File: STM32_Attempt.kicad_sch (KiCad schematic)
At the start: 29 parts, among them J1 Conn_01x04_Male, J2 Conn_01x04_Male, J3 Conn_01x04_Male, J4 Conn_01x04_Male, J5 USB_B_Micro, SW1 SW_SPDT, U1 AMS1117-3.3, U2 STM32F103C8T6, Y1 16Mhz

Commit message: added some leds
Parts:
- added D? (x4): WS2812B, LED_SMD:LED_WS2812B_PLCC4_5.0x5.0mm_P3.2mm, symbol LED:WS2812B
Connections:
- new net: D?.2 (DOUT), D?.4 (DIN) (x3)
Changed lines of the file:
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@@
+    (stroke (width 0) (type default) (color 0 0 0 0))
+  )
+  (wire (pts (xy 38.1 144.78) (xy 40.64 144.78))
     (stroke (width 0) (type default) (color 0 0 0 0))
   )
@@
     (stroke (width 0) (type default) (color 0 0 0 0))
   )
+  (wire (pts (xy 20.32 144.78) (xy 22.86 144.78))
+    (stroke (width 0) (type default) (color 0 0 0 0))
+  )
   (wire (pts (xy 111.76 69.85) (xy 123.19 69.85))
     (stroke (width 0) (type default) (color 0 0 0 0))
@@
   )
   (polyline (pts (xy 20.32 78.74) (xy 69.85 78.74))
+    (stroke (width 0) (type default) (color 0 0 0 0))
+  )
+  (wire (pts (xy 55.88 144.78) (xy 58.42 144.78))
     (stroke (width 0) (type default) (color 0 0 0 0))
   )
@@
     )
     (pin "1")
+  )
+  (symbol (lib_id "LED:WS2812B") (at 66.04 144.78 0) (unit 1)
+    (in_bom yes) (on_board yes) (fields_autoplaced)
+    (property "Reference" "D?" (id 0) (at 77.47 140.4493 0))
+    (property "Value" "WS2812B" (id 1) (at 77.47 142.9893 0))
+    (property "Footprint" "LED_SMD:LED_WS2812B_PLCC4_5.0x5.0mm_P3.2mm" (id 2) (at 67.31 152.4 0)
+      (effects (font (size 1.27 1.27)) (justify left top) hide)
+    )
+    (property "Datasheet" "https://cdn-shop.adafruit.com/datasheets/WS2812B.pdf" (id 3) (at 68.58 154.305 0)
+      (effects (font (size 1.27 1.27)) (justify left top) hide)
+    )
+    (pin "1")
+    (pin "2")
+    (pin "3")
+    (pin "4")
   )
   (symbol (lib_id "power:+3.3V") (at 116.84 139.7 0) (unit 1)
@@
     (pin "1")
   )
+  (symbol (lib_id "LED:WS2812B") (at 30.48 144.78 0) (unit 1)
+    (in_bom yes) (on_board yes) (fields_autoplaced)
+    (property "Reference" "D?" (id 0) (at 41.91 140.4493 0))
+    (property "Value" "WS2812B" (id 1) (at 41.91 142.9893 0))
+    (property "Footprint" "LED_SMD:LED_WS2812B_PLCC4_5.0x5.0mm_P3.2mm" (id 2) (at 31.75 152.4 0)
+      (effects (font (size 1.27 1.27)) (justify left top) hide)
+    )
+    (property "Datasheet" "https://cdn-shop.adafruit.com/datasheets/WS2812B.pdf" (id 3) (at 33.02 154.305 0)
+      (effects (font (size 1.27 1.27)) (justify left top) hide)
+    )
+    (pin "1")
+    (pin "2")
+    (pin "3")
+    (pin "4")
+  )
   (symbol (lib_id "Connector:Conn_01x04_Male") (at 109.22 123.19 0) (unit 1)
     (in_bom yes) (on_board yes)
@@
     (property "Datasheet" "~" (id 3) (at 109.22 123.19 0)
       (effects (font (size 1.27 1.27)) hide)
+    )
+    (pin "1")
+    (pin "2")
+    (pin "3")
+    (pin "4")
+  )
+  (symbol (lib_id "LED:WS2812B") (at 12.7 144.78 0) (unit 1)
+    (in_bom yes) (on_board yes) (fields_autoplaced)
+    (property "Reference" "D?" (id 0) (at 24.13 140.4493 0))
+    (property "Value" "WS2812B" (id 1) (at 24.13 142.9893 0))
+    (property "Footprint" "LED_SMD:LED_WS2812B_PLCC4_5.0x5.0mm_P3.2mm" (id 2) (at 13.97 152.4 0)
+      (effects (font (size 1.27 1.27)) (justify left top) hide)
+    )
+    (property "Datasheet" "https://cdn-shop.adafruit.com/datasheets/WS2812B.pdf" (id 3) (at 15.24 154.305 0)
+      (effects (font (size 1.27 1.27)) (justify left top) hide)
     )
     (pin "1")
@@
     (pin "2")
   )
+  (symbol (lib_id "LED:WS2812B") (at 48.26 144.78 0) (unit 1)
+    (in_bom yes) (on_board yes) (fields_autoplaced)
+    (property "Reference" "D?" (id 0) (at 59.69 140.4493 0))
+    (property "Value" "WS2812B" (id 1) (at 59.69 142.9893 0))
+    (property "Footprint" "LED_SMD:LED_WS2812B_PLCC4_5.0x5.0mm_P3.2mm" (id 2) (at 49.53 152.4 0)
+      (effects (font (size 1.27 1.27)) (justify left top) hide)
+    )
+    (property "Datasheet" "https://cdn-shop.adafruit.com/datasheets/WS2812B.pdf" (id 3) (at 50.8 154.305 0)
+      (effects (font (size 1.27 1.27)) (justify left top) hide)
+    )
+    (pin "1")
+    (pin "2")
+    (pin "3")
+    (pin "4")
+  )
   (symbol (lib_id "Device:Crystal_GND24") (at 127 87.63 0) (unit 1)
     (in_bom yes) (on_board yes)
@@
       (reference "D1") (unit 1) (value "RED") (footprint "LED_SMD:LED_0603_1608Metric")
     )
+    (path "/4eff6cc9-a752-4648-bcf8-9735cd35d6cf"
+      (reference "D?") (unit 1) (value "WS2812B") (footprint "LED_SMD:LED_WS2812B_PLCC4_5.0x5.0mm_P3.2mm")
+    )
+    (path "/b643fd5e-31e0-4018-ad35-66a9d8220cd2"
+      (reference "D?") (unit 1) (value "WS2812B") (footprint "LED_SMD:LED_WS2812B_PLCC4_5.0x5.0mm_P3.2mm")
+    )
+    (path "/b718910d-5e7e-4b6b-8296-0ffdf283276d"
+      (reference "D?") (unit 1) (value "WS2812B") (footprint "LED_SMD:LED_WS2812B_PLCC4_5.0x5.0mm_P3.2mm")
+    )
+    (path "/f18ae84f-67e5-42ce-a84a-119c99da9cea"
+      (reference "D?") (unit 1) (value "WS2812B") (footprint "LED_SMD:LED_WS2812B_PLCC4_5.0x5.0mm_P3.2mm")
+    )
     (path "/747181f7-c7c1-464c-a385-7c72b8faff1e"

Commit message: LED Matrix before markings
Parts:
- removed D? (x3): WS2812B, LED_SMD:LED_WS2812B_PLCC4_5.0x5.0mm_P3.2mm, symbol LED:WS2812B
- added D10, D11, D12, D13, D14, D15, D16, D17, D18, D19, D20, D21, D22, D23, D24, D25, D26, D27, D28, D29, D3, D30, D31, D32, D33, D34, D35, D36, D37, D38, D39, D4, D40, D41, D42, D43, D44, D45, D46, D47, D48, D49, D5, D50, D51, D52, D53, D54, D55, D56, D57, D58, D59, D6, D60, D61, D62, D63, D64, D65, D7, D8, D9: WS2812B, LED_SMD:LED_WS2812B_PLCC4_5.0x5.0mm_P3.2mm, symbol LED:WS2812B
- added J6: Conn_01x02, symbol Connector_Generic:Conn_01x02
- gave numbers to parts that had none: 1
- renumbered C7 to C10, C8 to C3, C3 to C4, C9 to C5, C4 to C6, C5 to C7, C10 to C8, C6 to C9, J3 to J2, J2 to J3
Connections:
- net GND: now also D2.3 (VSS), D10.3 (VSS), D11.3 (VSS), D12.3 (VSS), D13.3 (VSS), D14.3 (VSS), D15.3 (VSS), D16.3 (VSS), D17.3 (VSS), D18.3 (VSS), D19.3 (VSS), D20.3 (VSS), D21.3 (VSS), D22.3 (VSS), D23.3 (VSS), D24.3 (VSS), D25.3 (VSS), D26.3 (VSS), D27.3 (VSS), D28.3 (VSS), D29.3 (VSS), D3.3 (VSS), D30.3 (VSS), D31.3 (VSS), D32.3 (VSS), D33.3 (VSS), D34.3 (VSS), D35.3 (VSS), D36.3 (VSS), D37.3 (VSS), D38.3 (VSS), D39.3 (VSS), D4.3 (VSS), D40.3 (VSS), D41.3 (VSS), D42.3 (VSS), D43.3 (VSS), D44.3 (VSS), D45.3 (VSS), D46.3 (VSS), D47.3 (VSS), D48.3 (VSS), D49.3 (VSS), D5.3 (VSS), D50.3 (VSS), D51.3 (VSS), D52.3 (VSS), D53.3 (VSS), D54.3 (VSS), D55.3 (VSS), D56.3 (VSS), D57.3 (VSS), D58.3 (VSS), D59.3 (VSS), D6.3 (VSS), D60.3 (VSS), D61.3 (VSS), D62.3 (VSS), D63.3 (VSS), D64.3 (VSS), D65.3 (VSS), D7.3 (VSS), D8.3 (VSS), D9.3 (VSS), J6.2 (Pin_2)
- net at D2.2 (DOUT): now also D10.4 (DIN)
- net 5V: now reaches D2.1 (VDD)
- net 5V: now also D10.1 (VDD), D11.1 (VDD), D12.1 (VDD), D13.1 (VDD), D14.1 (VDD), D15.1 (VDD), D16.1 (VDD), D17.1 (VDD), D18.1 (VDD), D19.1 (VDD), D20.1 (VDD), D21.1 (VDD), D22.1 (VDD), D23.1 (VDD), D24.1 (VDD), D25.1 (VDD), D26.1 (VDD), D27.1 (VDD), D28.1 (VDD), D29.1 (VDD), D3.1 (VDD), D30.1 (VDD), D31.1 (VDD), D32.1 (VDD), D33.1 (VDD), D34.1 (VDD), D35.1 (VDD), D36.1 (VDD), D37.1 (VDD), D38.1 (VDD), D39.1 (VDD), D4.1 (VDD), D40.1 (VDD), D41.1 (VDD), D42.1 (VDD), D43.1 (VDD), D44.1 (VDD), D45.1 (VDD), D46.1 (VDD), D47.1 (VDD), D48.1 (VDD), D49.1 (VDD), D5.1 (VDD), D50.1 (VDD), D51.1 (VDD), D52.1 (VDD), D53.1 (VDD), D54.1 (VDD), D55.1 (VDD), D56.1 (VDD), D57.1 (VDD), D58.1 (VDD), D59.1 (VDD), D6.1 (VDD), D60.1 (VDD), D61.1 (VDD), D62.1 (VDD), D63.1 (VDD), D64.1 (VDD), D65.1 (VDD), D7.1 (VDD), D8.1 (VDD), D9.1 (VDD)
- net at D2.4 (DIN): now also U2.29 (PA8)
- new net: D16.2 (DOUT), D24.4 (DIN)
- new net: D16.4 (DIN), D8.2 (DOUT)
- new net: D7.2 (DOUT), D8.4 (DIN)
- new net: D15.2 (DOUT), D7.4 (DIN)
- new net: D33.4 (DIN), D41.2 (DOUT)
- new net: D41.4 (DIN), D49.2 (DOUT)
- new net: D47.4 (DIN), D55.2 (DOUT)
- new net: D55.4 (DIN), D63.2 (DOUT)
- new net: D24.2 (DOUT), D32.4 (DIN)
- new net: D37.4 (DIN), D45.2 (DOUT)
- new net: D45.4 (DIN), D53.2 (DOUT)
- new net: D49.4 (DIN), D57.2 (DOUT)
- new net: D11.4 (DIN), D19.2 (DOUT)
- new net: D19.4 (DIN), D27.2 (DOUT)
- new net: D29.4 (DIN), D37.2 (DOUT)
- new net: D42.2 (DOUT), D50.4 (DIN)
- new net: D34.2 (DOUT), D42.4 (DIN)
- new net: D22.2 (DOUT), D30.4 (DIN)
- new net: D14.2 (DOUT), D22.4 (DIN)
- new net: D21.4 (DIN), D29.2 (DOUT)
- new net: D14.4 (DIN), D6.2 (DOUT)
- new net: D5.2 (DOUT), D6.4 (DIN)
- new net: D20.2 (DOUT), D28.4 (DIN)
- new net: D12.2 (DOUT), D20.4 (DIN)
- new net: D46.2 (DOUT), D54.4 (DIN)
- new net: D38.2 (DOUT), D46.4 (DIN)
- new net: D40.2 (DOUT), D48.4 (DIN)
- new net: D32.2 (DOUT), D40.4 (DIN)
- new net: D53.4 (DIN), D61.2 (DOUT)
- new net: D30.2 (DOUT), D38.4 (DIN)
- new net: D62.2 (DOUT), D63.4 (DIN)
- new net: D54.2 (DOUT), D62.4 (DIN)
- new net: D26.2 (DOUT), D34.4 (DIN)
- new net: D18.2 (DOUT), D26.4 (DIN)
- new net: D48.2 (DOUT), D56.4 (DIN)
- new net: D56.2 (DOUT), D64.4 (DIN)
- new net: D44.2 (DOUT), D52.4 (DIN)
- new net: D36.2 (DOUT), D44.4 (DIN)
- new net: D17.2 (DOUT), D9.4 (DIN)
- new net: D17.4 (DIN), D25.2 (DOUT)
- new net: D25.4 (DIN), D33.2 (DOUT)
- new net: D60.2 (DOUT), D61.4 (DIN)
- new net: D52.2 (DOUT), D60.4 (DIN)
- new net: D64.2 (DOUT), D65.4 (DIN)
- new net: D35.4 (DIN), D43.2 (DOUT)
- new net: D43.4 (DIN), D51.2 (DOUT)
- new net: D57.4 (DIN), D65.2 (DOUT)
- new net: D12.4 (DIN), D4.2 (DOUT)
- new net: D50.2 (DOUT), D58.4 (DIN)
- new net: D27.4 (DIN), D35.2 (DOUT)
- new net: D3.2 (DOUT), D4.4 (DIN)
- new net: D11.2 (DOUT), D3.4 (DIN)
- new net: D58.2 (DOUT), D59.4 (DIN)
- new net: D51.4 (DIN), D59.2 (DOUT)
- new net: D15.4 (DIN), D23.2 (DOUT)
- new net: D23.4 (DIN), D31.2 (DOUT)
- new net: D31.4 (DIN), D39.2 (DOUT)
- new net: D10.2 (DOUT), D18.4 (DIN)
- new net: D28.2 (DOUT), D36.4 (DIN)
- new net: D39.4 (DIN), D47.2 (DOUT)
- new net: D13.2 (DOUT), D5.4 (DIN)
- new net: D13.4 (DIN), D21.2 (DOUT)
- new net +5V: J6.1 (Pin_1)
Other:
- moved on the sheet: D2

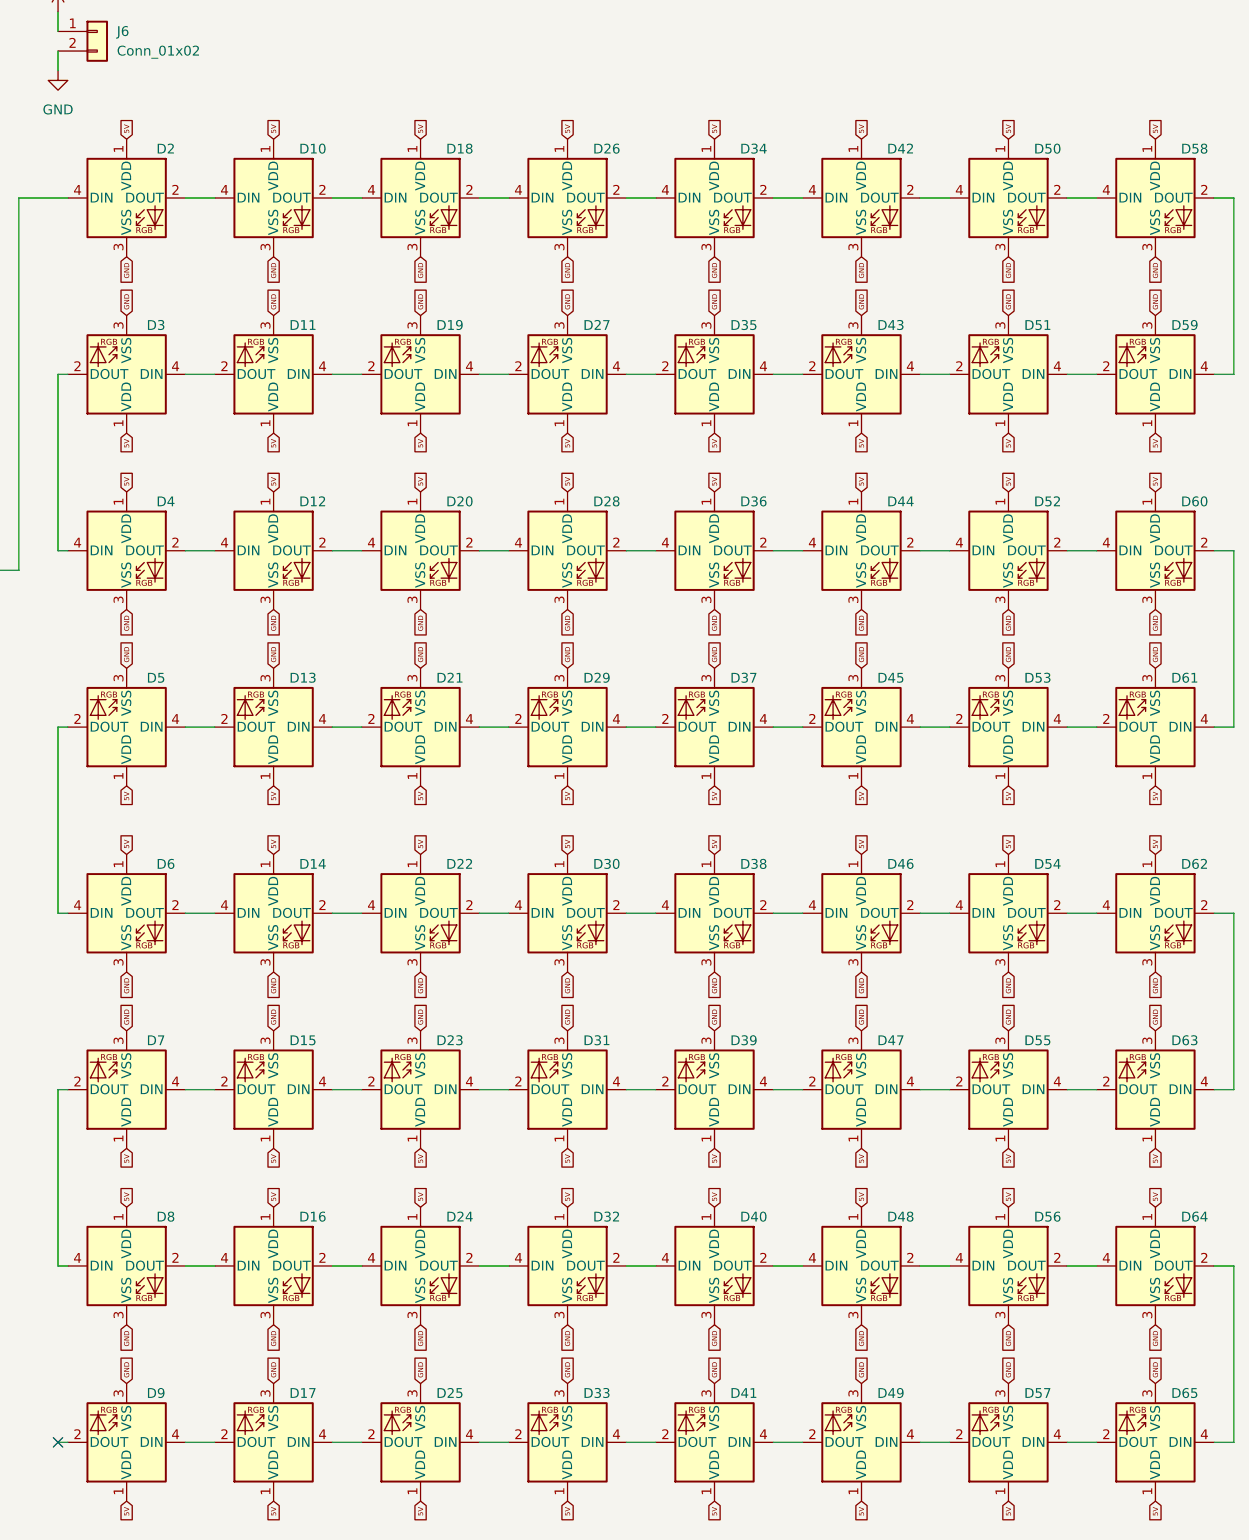
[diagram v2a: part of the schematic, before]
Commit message: renamed leds
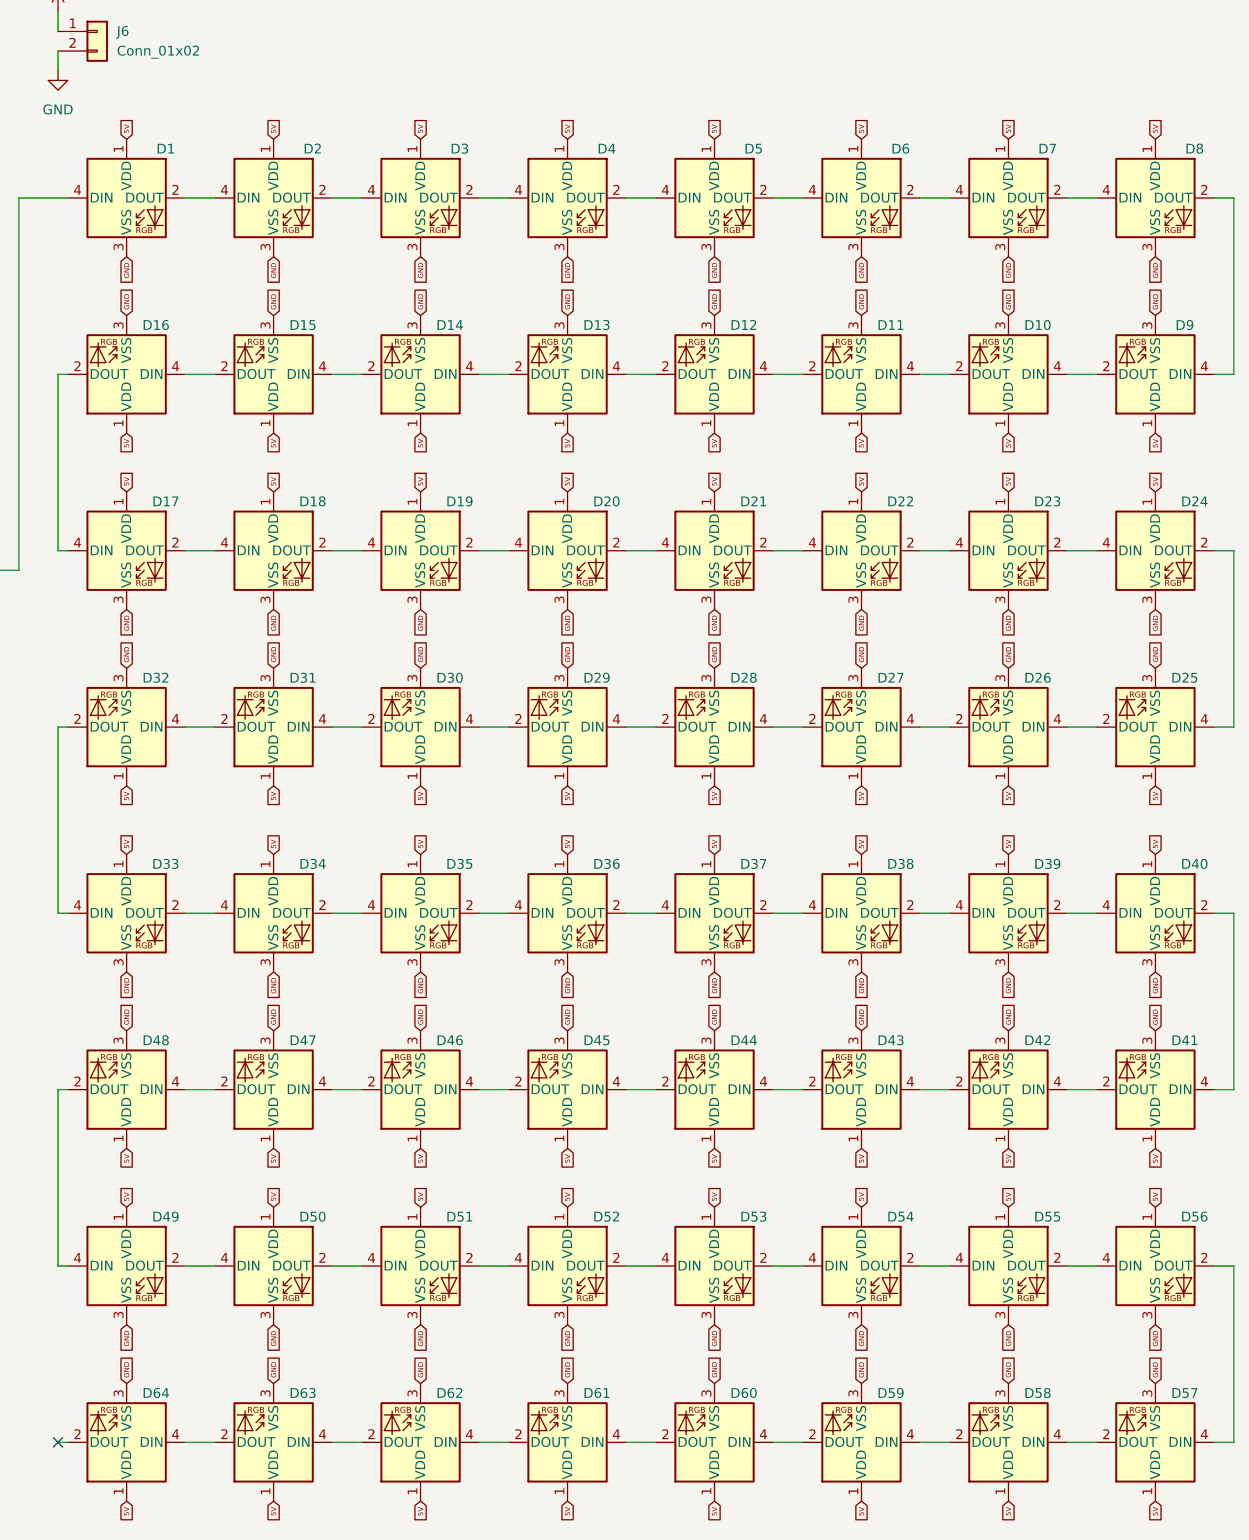
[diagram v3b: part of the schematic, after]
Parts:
- renumbered D2 to D1, D51 to D10, D43 to D11, D35 to D12, D27 to D13, D19 to D14, D11 to D15, D3 to D16, D4 to D17, D12 to D18, D20 to D19, D10 to D2, D28 to D20, D36 to D21, D44 to D22, D52 to D23, D60 to D24, D61 to D25, D53 to D26, D45 to D27, D37 to D28, D18 to D3, D21 to D30, D13 to D31, D5 to D32, D6 to D33, D14 to D34, D22 to D35, D30 to D36, D38 to D37, D46 to D38, D54 to D39, D26 to D4, D62 to D40, D63 to D41, D55 to D42, D47 to D43, D39 to D44, D31 to D45, D23 to D46, D15 to D47, D7 to D48, D8 to D49, D34 to D5, D16 to D50, D24 to D51, D32 to D52, D40 to D53, D48 to D54, D56 to D55, D64 to D56, D65 to D57, D57 to D58, D49 to D59, D42 to D6, D41 to D60, D33 to D61, D25 to D62, D17 to D63, D9 to D64, D50 to D7, D58 to D8, D59 to D9

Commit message: D16 VDD Error for review
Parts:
- renumbered D1 to D0
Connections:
- net 5V is gone; now on net +5V: D1.1 (VDD), D10.1 (VDD), D11.1 (VDD), D12.1 (VDD), D13.1 (VDD), D14.1 (VDD), D15.1 (VDD), D16.1 (VDD), D17.1 (VDD), D18.1 (VDD), D19.1 (VDD), D2.1 (VDD), D20.1 (VDD), D21.1 (VDD), D22.1 (VDD), D23.1 (VDD), D24.1 (VDD), D25.1 (VDD), D26.1 (VDD), D27.1 (VDD), D28.1 (VDD), D29.1 (VDD), D3.1 (VDD), D30.1 (VDD), D31.1 (VDD), D32.1 (VDD), D33.1 (VDD), D34.1 (VDD), D35.1 (VDD), D36.1 (VDD), D37.1 (VDD), D38.1 (VDD), D39.1 (VDD), D4.1 (VDD), D40.1 (VDD), D41.1 (VDD), D42.1 (VDD), D43.1 (VDD), D44.1 (VDD), D45.1 (VDD), D46.1 (VDD), D47.1 (VDD), D48.1 (VDD), D49.1 (VDD), D5.1 (VDD), D50.1 (VDD), D51.1 (VDD), D52.1 (VDD), D53.1 (VDD), D54.1 (VDD), D55.1 (VDD), D56.1 (VDD), D57.1 (VDD), D58.1 (VDD), D59.1 (VDD), D6.1 (VDD), D60.1 (VDD), D61.1 (VDD), D62.1 (VDD), D63.1 (VDD), D64.1 (VDD), D7.1 (VDD), D8.1 (VDD), D9.1 (VDD)
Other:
- moved on the sheet: D33, D34, D35, D36, D37, D38, D39, D40, D41, D42, D43, D44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

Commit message: 19/10/12 session end
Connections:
- net +5V renamed power flag
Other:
- note added: "LED Matrix Arrangement"
